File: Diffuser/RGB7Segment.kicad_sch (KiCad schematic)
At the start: 2 parts, among them J1 Conn_01x02_Socket, J2 Conn_01x02_Socket

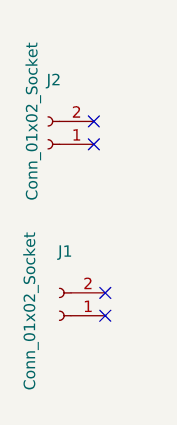
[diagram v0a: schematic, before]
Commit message: Working 7 Segment Layout
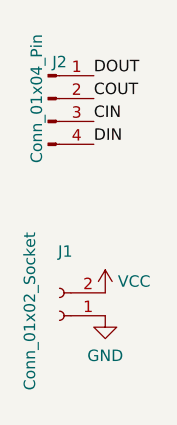
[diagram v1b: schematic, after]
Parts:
- removed J2: Conn_01x02_Socket, Connector_PinHeader_1.27mm:PinHeader_1x02_P1.27mm_Vertical, symbol Connector:Conn_01x02_Socket
- added J2: Conn_01x04_Pin, Connector_PinHeader_1.27mm:PinHeader_1x04_P1.27mm_Vertical, symbol Connector:Conn_01x04_Pin
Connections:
- net GND: now reaches J1.1 (Pin_1)
- net VCC: now reaches J1.2 (Pin_2)
- new net CIN: J2.3 (Pin_3)
- new net COUT: J2.2 (Pin_2)
- new net DIN: J2.4 (Pin_4)
- new net DOUT: J2.1 (Pin_1)
- no-connect marks 4 -> 0
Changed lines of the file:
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@@
 	(generator_version "8.0")
 	(paper "A4")
-	(no_connect
-		(at 27.94 57.15)
-	)
-	(no_connect
-		(at 26.67 38.1)
-	)
-	(no_connect
-		(at 26.67 35.56)
-	)
-	(no_connect
-		(at 27.94 54.61)
+	(label "DIN"
+		(at 26.67 38.1 0)
+		(fields_autoplaced yes)
+		(effects
+			(font
+				(size 1.27 1.27)
+			)
+			(justify left bottom)
+		)
+	)
+	(label "DOUT"
+		(at 26.67 30.48 0)
+		(fields_autoplaced yes)
+		(effects
+			(font
+				(size 1.27 1.27)
+			)
+			(justify left bottom)
+		)
+	)
+	(label "CIN"
+		(at 26.67 35.56 0)
+		(fields_autoplaced yes)
+		(effects
+			(font
+				(size 1.27 1.27)
+			)
+			(justify left bottom)
+		)
+	)
+	(label "COUT"
+		(at 26.67 33.02 0)
+		(fields_autoplaced yes)
+		(effects
+			(font
+				(size 1.27 1.27)
+			)
+			(justify left bottom)
+		)
 	)
 	(symbol
@@
 	)
 	(symbol
-		(lib_id "Connector:Conn_01x02_Socket")
-		(at 21.59 38.1 180)
+		(lib_id "power:GND")
+		(at 27.94 57.15 0)
+		(unit 1)
+		(exclude_from_sim no)
+		(in_bom yes)
+		(on_board yes)
+		(dnp no)
+		(fields_autoplaced yes)
+		(property "Reference" "#PWR0104"
+			(at 27.94 63.5 0)
+			(effects
+				(font
+					(size 1.27 1.27)
+				)
+				(hide yes)
+			)
+		)
+		(property "Value" "GND"
+			(at 27.94 61.5934 0)
+			(effects
+				(font
+					(size 1.27 1.27)
+				)
+			)
+		)
+		(property "Footprint" ""
+			(at 27.94 57.15 0)
+			(effects
+				(font
+					(size 1.27 1.27)
+				)
+				(hide yes)
+			)
+		)
+		(property "Datasheet" ""
+			(at 27.94 57.15 0)
+			(effects
+				(font
+					(size 1.27 1.27)
+				)
+				(hide yes)
+			)
+		)
+		(property "Description" ""
+			(at 27.94 57.15 0)
+			(effects
+				(font
+					(size 1.27 1.27)
+				)
+				(hide yes)
+			)
+		)
+		(pin "1"
+		)
+		(instances
+			(project ""
+				(path "/2de6dca9-f910-47a3-9fba-0aaf6ef710f6"
+					(reference "#PWR0104")
+					(unit 1)
+				)
+			)
+		)
+	)
+	(symbol
+		(lib_id "Connector:Conn_01x04_Pin")
+		(at 21.59 33.02 0)
 		(unit 1)
 		(exclude_from_sim no)
@@
 		(dnp no)
 		(property "Reference" "J2"
-			(at 22.225 30.9583 0)
-			(effects
-				(font
-					(size 1.27 1.27)
-				)
-			)
-		)
-		(property "Value" "Conn_01x02_Socket"
-			(at 19.812 35.56 90)
-			(effects
-				(font
-					(size 1.27 1.27)
-				)
-			)
-		)
-		(property "Footprint" "Connector_PinHeader_1.27mm:PinHeader_1x02_P1.27mm_Vertical"
-			(at 21.59 38.1 0)
+			(at 22.86 28.956 0)
+			(effects
+				(font
+					(size 1.27 1.27)
+				)
+			)
+		)
+		(property "Value" "Conn_01x04_Pin"
+			(at 20.32 33.02 90)
+			(effects
+				(font
+					(size 1.27 1.27)
+				)
+			)
+		)
+		(property "Footprint" "Connector_PinHeader_1.27mm:PinHeader_1x04_P1.27mm_Vertical"
+			(at 21.59 33.02 0)
 			(effects
 				(font
@@
 		)
 		(property "Datasheet" "~"
-			(at 21.59 38.1 0)
-			(effects
-				(font
-					(size 1.27 1.27)
-				)
-				(hide yes)
-			)
-		)
-		(property "Description" "Generic connector, single row, 01x02, script generated"
-			(at 21.59 38.1 0)
-			(effects
-				(font
-					(size 1.27 1.27)
-				)
-				(hide yes)
-			)
+			(at 21.59 33.02 0)
+			(effects
+				(font
+					(size 1.27 1.27)
+				)
+				(hide yes)
+			)
+		)
+		(property "Description" "Generic connector, single row, 01x04, script generated"
+			(at 21.59 33.02 0)
+			(effects
+				(font
+					(size 1.27 1.27)
+				)
+				(hide yes)
+			)
+		)
+		(pin "2"
 		)
 		(pin "1"
 		)
-		(pin "2"
+		(pin "3"
+		)
+		(pin "4"
 		)
 		(instances
@@
 					(unit 1)
 				)
+			)
+		)
+	)
+	(symbol
+		(lib_id "power:VCC")
+		(at 27.94 54.61 0)
+		(unit 1)
+		(exclude_from_sim no)
+		(in_bom yes)
+		(on_board yes)
+		(dnp no)
+		(fields_autoplaced yes)
+		(property "Reference" "#PWR0127"
+			(at 27.94 58.42 0)
+			(effects
+				(font
+					(size 1.27 1.27)
+				)
+				(hide yes)
+			)
+		)
+		(property "Value" "VCC"
+			(at 29.337 53.34 0)
+			(effects
+				(font
+					(size 1.27 1.27)
+				)
+				(justify left)
+			)
+		)
+		(property "Footprint" ""
+			(at 27.94 54.61 0)
+			(effects
+				(font
+					(size 1.27 1.27)
+				)
+				(hide yes)
+			)
+		)
+		(property "Datasheet" ""
+			(at 27.94 54.61 0)
+			(effects
+				(font
+					(size 1.27 1.27)
+				)
+				(hide yes)
+			)
+		)
+		(property "Description" ""
+			(at 27.94 54.61 0)
+			(effects
+				(font
+					(size 1.27 1.27)
+				)
+				(hide yes)
+			)
+		)
+		(pin "1"
+		)
+		(instances
+			(project ""
+				(path "/2de6dca9-f910-47a3-9fba-0aaf6ef710f6"
+					(reference "#PWR0127")
+					(unit 1)
+				)
